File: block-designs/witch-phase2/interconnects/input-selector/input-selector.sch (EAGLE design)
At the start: 37 parts, among them IC1 74LVC1G17DBV, IC10 74LVC1G17DBV, IC11 74LVC1G17DBV, IC12 74LVC1G17DBV, IC13 74LVC1G17DBV, IC14 74LVC1G17DBV, IC2 74LVC1G17DBV, IC3 74LVC1G17DBV, IC4 74LVC1G17DBV, IC5 74LVC1G17DBV, IC6 74LVC1G17DBV, IC7 74LVC1G17DBV, IC8 74LVC1G17DBV, IC9 74LVC1G17DBV

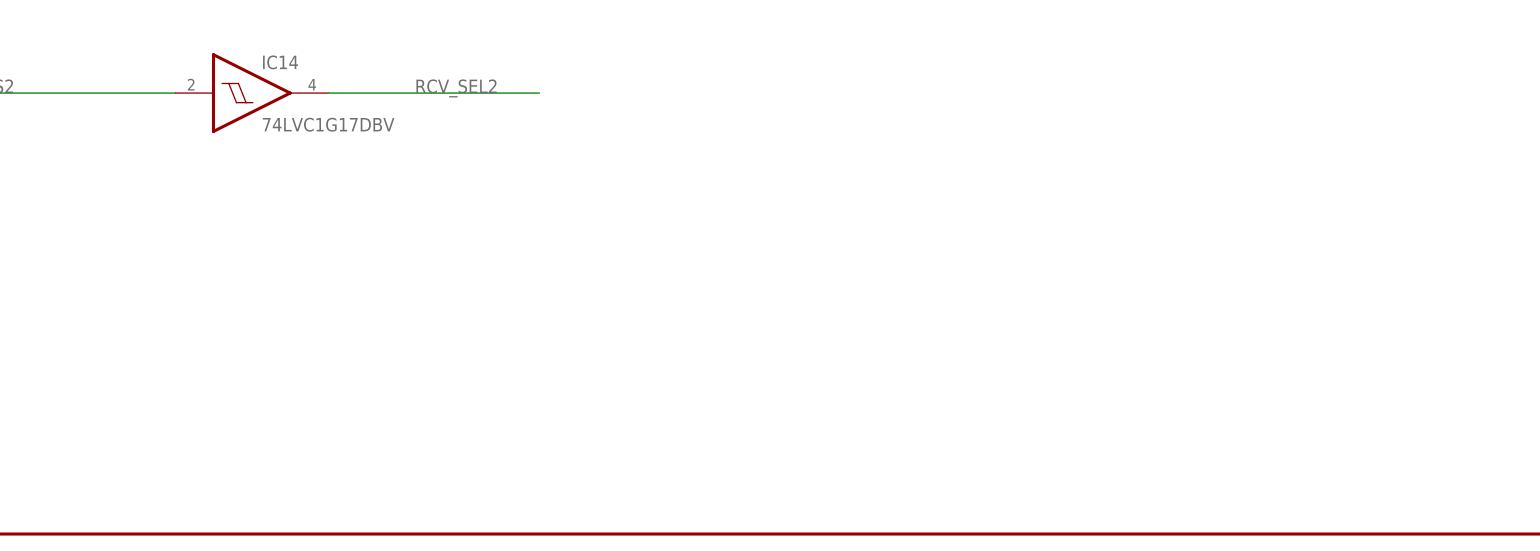
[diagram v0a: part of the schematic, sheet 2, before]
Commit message: schematic cleanup and change bypass caps from 0805 to 0603
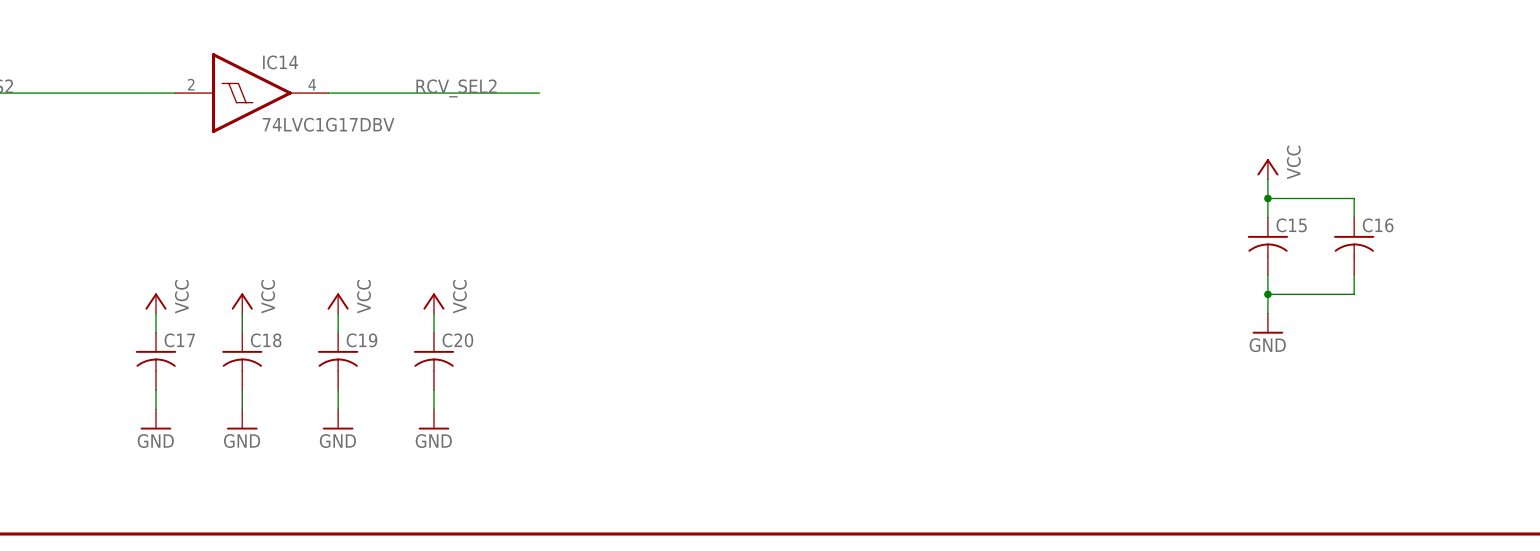
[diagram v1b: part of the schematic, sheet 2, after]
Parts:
- added C15, C16: (no value), resistor:C-USC0805
- added C17, C18, C19, C20: (no value), resistor:C-USC0603
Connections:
- net GND: now also C15.2, C16.2, C17.2, C18.2, C19.2, C20.2
- net VCC: now also C15.1, C16.1, C17.1, C18.1, C19.1, C20.1
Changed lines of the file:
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@@
 <setting verticaltext="up"/>
 </settings>
-<grid distance="0.1" unitdist="inch" unit="inch" style="dots" multiple="1" display="no" altdistance="0.01" altunitdist="inch" altunit="inch"/>
+<grid distance="0.05" unitdist="inch" unit="inch" style="dots" multiple="1" display="no" altdistance="0.01" altunitdist="inch" altunit="inch"/>
 <layers>
 <layer number="1" name="Top" color="4" fill="1" visible="no" active="no"/>
@@
 <part name="JP4" library="custom-pinhead" deviceset="PINHD-1X6" device=""/>
 <part name="GND18" library="supply1" deviceset="GND" device=""/>
+<part name="C15" library="resistor" deviceset="C-US" device="C0805"/>
+<part name="P+17" library="supply1" deviceset="VCC" device=""/>
+<part name="GND23" library="supply1" deviceset="GND" device=""/>
+<part name="C16" library="resistor" deviceset="C-US" device="C0805"/>
+<part name="C17" library="resistor" deviceset="C-US" device="C0603"/>
+<part name="P+18" library="supply1" deviceset="VCC" device=""/>
+<part name="GND24" library="supply1" deviceset="GND" device=""/>
+<part name="C18" library="resistor" deviceset="C-US" device="C0603"/>
+<part name="P+19" library="supply1" deviceset="VCC" device=""/>
+<part name="GND25" library="supply1" deviceset="GND" device=""/>
+<part name="C19" library="resistor" deviceset="C-US" device="C0603"/>
+<part name="P+20" library="supply1" deviceset="VCC" device=""/>
+<part name="GND26" library="supply1" deviceset="GND" device=""/>
+<part name="C20" library="resistor" deviceset="C-US" device="C0603"/>
+<part name="P+21" library="supply1" deviceset="VCC" device=""/>
+<part name="GND27" library="supply1" deviceset="GND" device=""/>
 </parts>
 <sheets>
@@
 <instance part="JP4" gate="A" x="224.79" y="107.95" rot="MR180"/>
 <instance part="GND18" gate="1" x="208.28" y="92.71"/>
+<instance part="C15" gate="G$1" x="204.47" y="39.37"/>
+<instance part="P+17" gate="VCC" x="204.47" y="49.53" rot="MR0"/>
+<instance part="GND23" gate="1" x="204.47" y="26.67"/>
+<instance part="C16" gate="G$1" x="215.9" y="39.37"/>
+<instance part="C17" gate="G$1" x="57.15" y="24.13"/>
+<instance part="P+18" gate="VCC" x="57.15" y="31.75" rot="MR0"/>
+<instance part="GND24" gate="1" x="57.15" y="13.97"/>
+<instance part="C18" gate="G$1" x="68.58" y="24.13"/>
+<instance part="P+19" gate="VCC" x="68.58" y="31.75" rot="MR0"/>
+<instance part="GND25" gate="1" x="68.58" y="13.97"/>
+<instance part="C19" gate="G$1" x="81.28" y="24.13"/>
+<instance part="P+20" gate="VCC" x="81.28" y="31.75" rot="MR0"/>
+<instance part="GND26" gate="1" x="81.28" y="13.97"/>
+<instance part="C20" gate="G$1" x="93.98" y="24.13"/>
+<instance part="P+21" gate="VCC" x="93.98" y="31.75" rot="MR0"/>
+<instance part="GND27" gate="1" x="93.98" y="13.97"/>
 </instances>
 <busses>
@@
 <pinref part="GND18" gate="1" pin="GND"/>
 </segment>
+<segment>
+<pinref part="GND23" gate="1" pin="GND"/>
+<pinref part="C15" gate="G$1" pin="2"/>
+<wire x1="204.47" y1="29.21" x2="204.47" y2="31.75" width="0.1524" layer="91"/>
+<pinref part="C16" gate="G$1" pin="2"/>
+<wire x1="204.47" y1="31.75" x2="204.47" y2="34.29" width="0.1524" layer="91"/>
+<wire x1="215.9" y1="34.29" x2="215.9" y2="31.75" width="0.1524" layer="91"/>
+<wire x1="215.9" y1="31.75" x2="204.47" y2="31.75" width="0.1524" layer="91"/>
+<junction x="204.47" y="31.75"/>
+</segment>
+<segment>
+<wire x1="57.15" y1="19.05" x2="57.15" y2="16.51" width="0.1524" layer="91"/>
+<pinref part="GND24" gate="1" pin="GND"/>
+<pinref part="C17" gate="G$1" pin="2"/>
+</segment>
+<segment>
+<wire x1="68.58" y1="19.05" x2="68.58" y2="16.51" width="0.1524" layer="91"/>
+<pinref part="GND25" gate="1" pin="GND"/>
+<pinref part="C18" gate="G$1" pin="2"/>
+</segment>
+<segment>
+<wire x1="81.28" y1="19.05" x2="81.28" y2="16.51" width="0.1524" layer="91"/>
+<pinref part="GND26" gate="1" pin="GND"/>
+<pinref part="C19" gate="G$1" pin="2"/>
+</segment>
+<segment>
+<wire x1="93.98" y1="19.05" x2="93.98" y2="16.51" width="0.1524" layer="91"/>
+<pinref part="GND27" gate="1" pin="GND"/>
+<pinref part="C20" gate="G$1" pin="2"/>
+</segment>
 </net>
 <net name="VCC" class="0">
@@
 <pinref part="C9" gate="G$1" pin="1"/>
 </segment>
-</net>
+<segment>
+<pinref part="C15" gate="G$1" pin="1"/>
+<pinref part="P+17" gate="VCC" pin="VCC"/>
+<wire x1="204.47" y1="41.91" x2="204.47" y2="44.45" width="0.1524" layer="91"/>
+<pinref part="C16" gate="G$1" pin="1"/>
+<wire x1="204.47" y1="44.45" x2="204.47" y2="46.99" width="0.1524" layer="91"/>
+<wire x1="215.9" y1="41.91" x2="215.9" y2="44.45" width="0.1524" layer="91"/>
+<wire x1="215.9" y1="44.45" x2="204.47" y2="44.45" width="0.1524" layer="91"/>
+<junction x="204.47" y="44.45"/>
+</segment>
+<segment>
+<wire x1="57.15" y1="26.67" x2="57.15" y2="29.21" width="0.1524" layer="91"/>
+<pinref part="P+18" gate="VCC" pin="VCC"/>
+<pinref part="C17" gate="G$1" pin="1"/>
+</segment>
+<segment>
+<wire x1="68.58" y1="26.67" x2="68.58" y2="29.21" width="0.1524" layer="91"/>
+<pinref part="P+19" gate="VCC" pin="VCC"/>
+<pinref part="C18" gate="G$1" pin="1"/>
+</segment>
+<segment>
+<wire x1="81.28" y1="26.67" x2="81.28" y2="29.21" width="0.1524" layer="91"/>
+<pinref part="P+20" gate="VCC" pin="VCC"/>
+<pinref part="C19" gate="G$1" pin="1"/>
+</segment>
+<segment>
+<wire x1="93.98" y1="26.67" x2="93.98" y2="29.21" width="0.1524" layer="91"/>
+<pinref part="P+21" gate="VCC" pin="VCC"/>
+<pinref part="C20" gate="G$1" pin="1"/>
+</segment>
+</net>

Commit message: add revision numbers
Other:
- note added: "R1"
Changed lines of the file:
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@@
 <sheet>
 <plain>
+<text x="392.43" y="7.62" size="1.778" layer="94">R1</text>
 </plain>
 <instances>
@@
 <sheet>
 <plain>
+<text x="393.7" y="7.62" size="1.778" layer="94">R1</text>
 </plain>
 <instances>
